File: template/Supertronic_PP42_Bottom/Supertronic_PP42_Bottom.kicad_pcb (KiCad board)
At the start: 2 copper layers, 52 x 65 mm, 4 parts

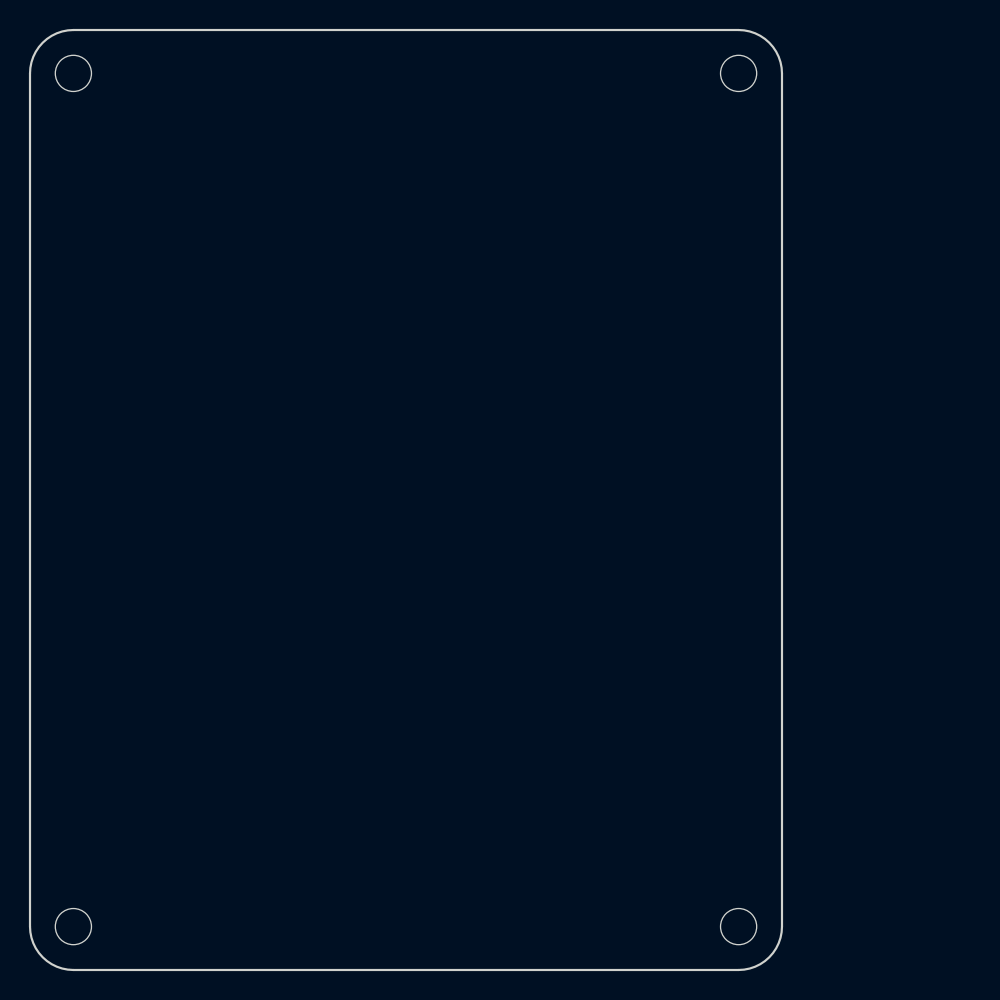
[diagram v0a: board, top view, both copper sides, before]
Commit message: Updated templates
Added mounting holes on schematics, dimensions and re-adjusted board
sizes
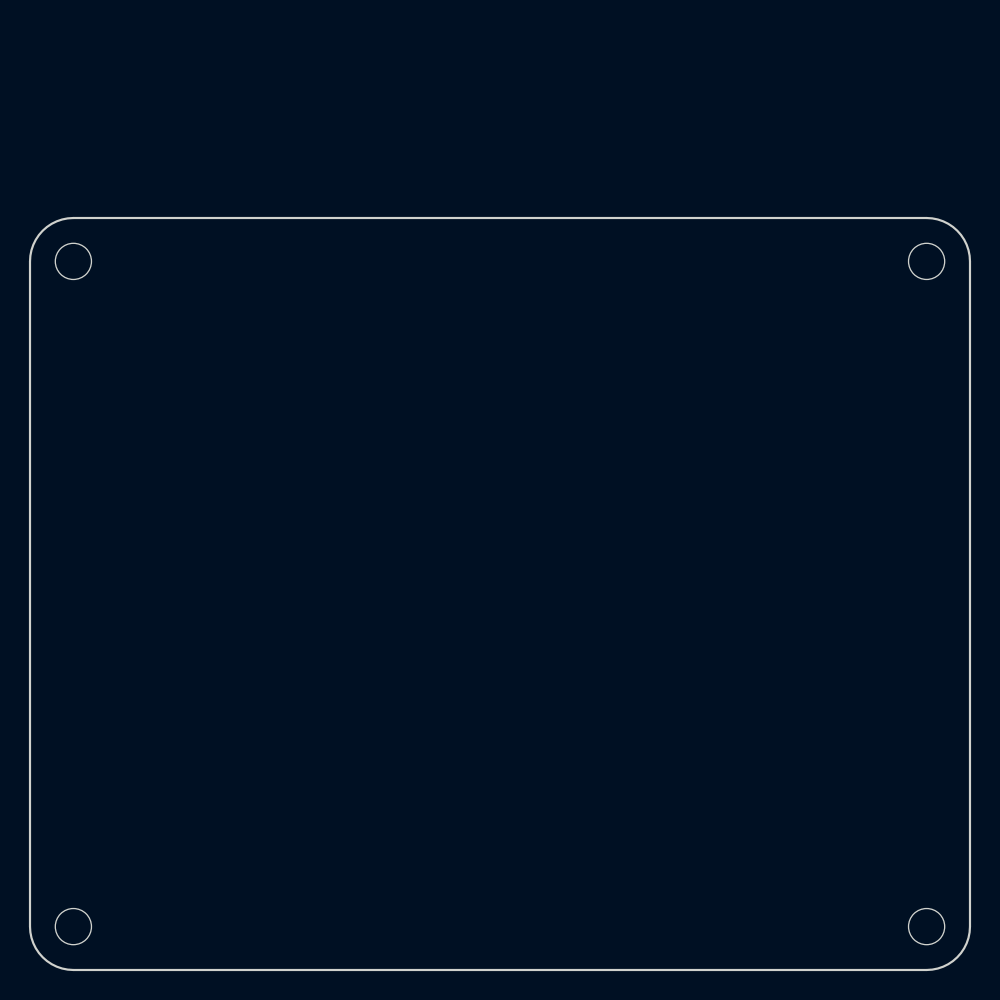
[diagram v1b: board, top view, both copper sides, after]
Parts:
- H1, H2, H3, H4: renamed from REF**; value MountingHole_2.5mm -> MountingHole
- moved H1 59.0 mm to (123.5, 122.5), turned to 90 degrees
- moved H4 59.0 mm to (182.5, 122.5), turned to 90 degrees
- moved H2 47.8 mm to (123.5, 76.5), turned to 90 degrees
- moved H3 47.8 mm to (182.5, 76.5), turned to 90 degrees
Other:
- board size 52 x 65 mm -> 65 x 52 mm
